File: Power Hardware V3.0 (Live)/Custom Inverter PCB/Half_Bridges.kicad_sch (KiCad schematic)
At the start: 27 parts, among them Q1 CSD19532Q5B, Q2 CSD19532Q5B, Q3 CSD19532Q5B, Q4 CSD19532Q5B, Q5 CSD19532Q5B, Q6 CSD19532Q5B

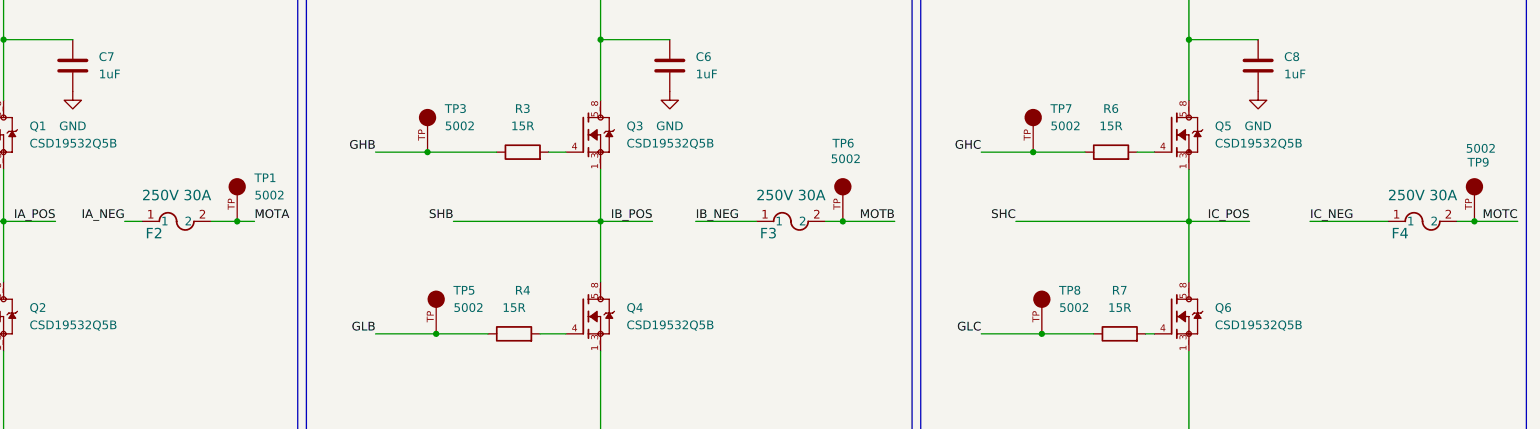
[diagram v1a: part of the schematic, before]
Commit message: PCB V3 changes
-HV outputs and inputs changed to screw terminals for lugs
- Fuses changes to 50A
- ADC pin for temp sense along with the temp sensing circuit
- Added more pins to motor encoder term for temp sense
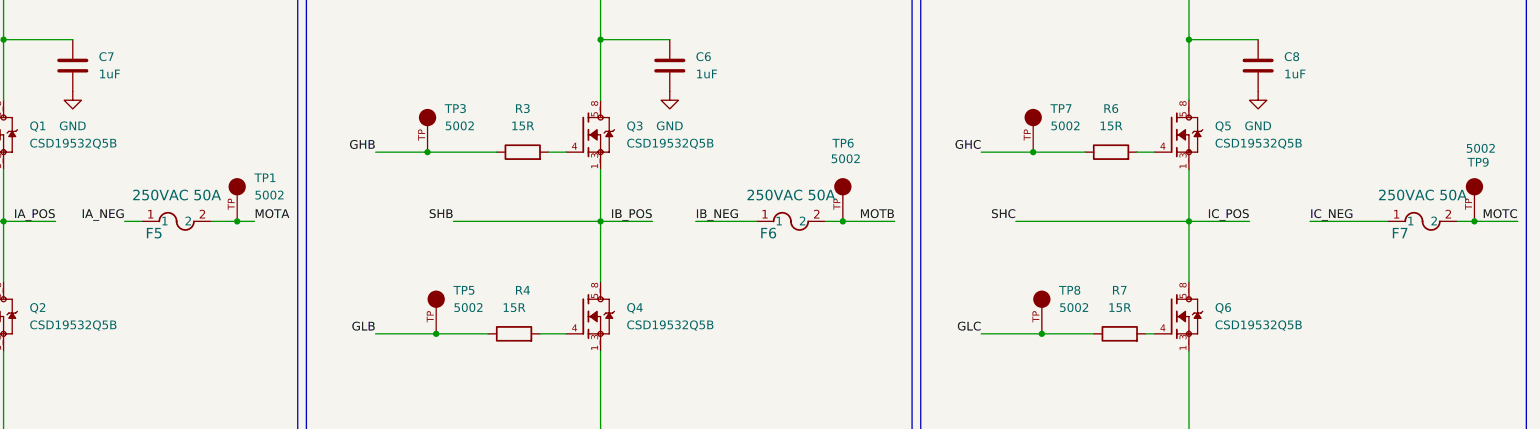
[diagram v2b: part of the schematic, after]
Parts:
- removed F2, F3, F4: 250V 30A, 0463030_ER:FUSE_0463_LTF-M, symbol 2025-02-24_21-09-15:0463030.ER
- added F5, F6, F7: 250VAC 50A, 0463030_ER:FUSE_0463_LTF-M, symbol 2025-02-24_21-09-15:0463030.ER
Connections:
- net IA_NEG: now also F5.1
- net IB_NEG: now also F6.1
- net IC_NEG: now also F7.1
- net MOTA: now also F5.2
- net MOTB: now also F6.2
- net MOTC: now also F7.2
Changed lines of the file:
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@@
-	)
-	(symbol
-		(lib_id "2025-02-24_21-09-15:0463030.ER")
-		(at 78.74 62.23 0)
-		(unit 1)
-		(exclude_from_sim no)
-		(in_bom yes)
-		(on_board yes)
-		(dnp no)
-		(property "Reference" "F2"
-			(at 80.518 64.008 0)
-			(effects
-				(font
-					(size 1.524 1.524)
-				)
-			)
-		)
-		(property "Value" "250V 30A"
-			(at 83.82 58.42 0)
-			(effects
-				(font
-					(size 1.524 1.524)
-				)
-			)
-		)
-		(property "Footprint" "0463030_ER:FUSE_0463_LTF-M"
-			(at 78.74 62.23 0)
-			(effects
-				(font
-					(size 1.27 1.27)
-					(italic yes)
-				)
-				(hide yes)
-			)
-		)
-		(property "Datasheet" "0463030.ER"
-			(at 78.74 62.23 0)
-			(effects
-				(font
-					(size 1.27 1.27)
-					(italic yes)
-				)
-				(hide yes)
-			)
-		)
-		(property "Description" "https://mm.digikey.com/Volume0/opasdata/d220001/medias/docus/1086/463_Series.pdf"
-			(at 78.74 62.23 0)
-			(effects
-				(font
-					(size 1.27 1.27)
-				)
-				(hide yes)
-			)
-		)
-		(property "Part Number" "0463030.ER"
-			(at 78.74 62.23 0)
-			(effects
-				(font
-					(size 1.27 1.27)
-				)
-				(hide yes)
-			)
-		)
-		(pin "2"
-		)
-		(pin "1"
-		)
-		(instances
-			(project "Custom Inverter PCB"
-				(path "/3e1046b6-e265-4cdd-8404-c358cfc105fe/dd00afae-8344-4250-8f9c-c68c6680e783"
-					(reference "F2")
-					(unit 1)
-				)
-			)
-		)
 	)
 	(symbol
@@
 	(symbol
 		(lib_id "2025-02-24_21-09-15:0463030.ER")
-		(at 168.91 62.23 0)
-		(unit 1)
-		(exclude_from_sim no)
-		(in_bom yes)
-		(on_board yes)
-		(dnp no)
-		(property "Reference" "F3"
-			(at 170.688 64.008 0)
+		(at 78.74 62.23 0)
+		(unit 1)
+		(exclude_from_sim no)
+		(in_bom yes)
+		(on_board yes)
+		(dnp no)
+		(property "Reference" "F5"
+			(at 80.518 64.008 0)
 			(effects
 				(font
@@
 			)
 		)
-		(property "Value" "250V 30A"
-			(at 173.99 58.42 0)
+		(property "Value" "250VAC 50A"
+			(at 83.82 58.42 0)
 			(effects
 				(font
@@
 		)
 		(property "Footprint" "0463030_ER:FUSE_0463_LTF-M"
-			(at 168.91 62.23 0)
+			(at 78.74 62.23 0)
 			(effects
 				(font
@@
 			)
 		)
-		(property "Datasheet" "0463030.ER"
-			(at 168.91 62.23 0)
+		(property "Datasheet" "https://www.bourns.com/docs/Product-Datasheets/SF-3812F-T.pdf"
+			(at 78.74 62.23 0)
 			(effects
 				(font
@@
 			)
 		)
-		(property "Description" "https://mm.digikey.com/Volume0/opasdata/d220001/medias/docus/1086/463_Series.pdf"
-			(at 168.91 62.23 0)
-			(effects
-				(font
-					(size 1.27 1.27)
-				)
-				(hide yes)
-			)
-		)
-		(property "Part Number" "0463030.ER"
-			(at 168.91 62.23 0)
+		(property "Description" "50A 250VAC, 100VDC"
+			(at 78.74 62.23 0)
+			(effects
+				(font
+					(size 1.27 1.27)
+				)
+				(hide yes)
+			)
+		)
+		(property "Part Number" "SF-3812F5000T-2"
+			(at 78.74 62.23 0)
 			(effects
 				(font
@@
 			(project "Custom Inverter PCB"
 				(path "/3e1046b6-e265-4cdd-8404-c358cfc105fe/dd00afae-8344-4250-8f9c-c68c6680e783"
-					(reference "F3")
+					(reference "F5")
 					(unit 1)
 				)
@@
 	)
 	(symbol
+		(lib_id "2025-02-24_21-09-15:0463030.ER")
+		(at 168.91 62.23 0)
+		(unit 1)
+		(exclude_from_sim no)
+		(in_bom yes)
+		(on_board yes)
+		(dnp no)
+		(property "Reference" "F6"
+			(at 170.688 64.008 0)
+			(effects
+				(font
+					(size 1.524 1.524)
+				)
+			)
+		)
+		(property "Value" "250VAC 50A"
+			(at 173.99 58.42 0)
+			(effects
+				(font
+					(size 1.524 1.524)
+				)
+			)
+		)
+		(property "Footprint" "0463030_ER:FUSE_0463_LTF-M"
+			(at 168.91 62.23 0)
+			(effects
+				(font
+					(size 1.27 1.27)
+					(italic yes)
+				)
+				(hide yes)
+			)
+		)
+		(property "Datasheet" "https://www.bourns.com/docs/Product-Datasheets/SF-3812F-T.pdf"
+			(at 168.91 62.23 0)
+			(effects
+				(font
+					(size 1.27 1.27)
+					(italic yes)
+				)
+				(hide yes)
+			)
+		)
+		(property "Description" "50A 250VAC, 100VDC"
+			(at 168.91 62.23 0)
+			(effects
+				(font
+					(size 1.27 1.27)
+				)
+				(hide yes)
+			)
+		)
+		(property "Part Number" "SF-3812F5000T-2"
+			(at 168.91 62.23 0)
+			(effects
+				(font
+					(size 1.27 1.27)
+				)
+				(hide yes)
+			)
+		)
+		(pin "2"
+		)
+		(pin "1"
+		)
+		(instances
+			(project "Custom Inverter PCB"
+				(path "/3e1046b6-e265-4cdd-8404-c358cfc105fe/dd00afae-8344-4250-8f9c-c68c6680e783"
+					(reference "F6")
+					(unit 1)
+				)
+			)
+		)
+	)
+	(symbol
 		(lib_id "5002:5002")
 		(at 121.92 73.66 90)
@@
 	)
 	(symbol
+		(lib_id "2025-02-24_21-09-15:0463030.ER")
+		(at 261.62 62.23 0)
+		(unit 1)
+		(exclude_from_sim no)
+		(in_bom yes)
+		(on_board yes)
+		(dnp no)
+		(property "Reference" "F7"
+			(at 263.398 64.008 0)
+			(effects
+				(font
+					(size 1.524 1.524)
+				)
+			)
+		)
+		(property "Value" "250VAC 50A"
+			(at 266.7 58.42 0)
+			(effects
+				(font
+					(size 1.524 1.524)
+				)
+			)
+		)
+		(property "Footprint" "0463030_ER:FUSE_0463_LTF-M"
+			(at 261.62 62.23 0)
+			(effects
+				(font
+					(size 1.27 1.27)
+					(italic yes)
+				)
+				(hide yes)
+			)
+		)
+		(property "Datasheet" "https://www.bourns.com/docs/Product-Datasheets/SF-3812F-T.pdf"
+			(at 261.62 62.23 0)
+			(effects
+				(font
+					(size 1.27 1.27)
+					(italic yes)
+				)
+				(hide yes)
+			)
+		)
+		(property "Description" "50A 250VAC, 100VDC"
+			(at 261.62 62.23 0)
+			(effects
+				(font
+					(size 1.27 1.27)
+				)
+				(hide yes)
+			)
+		)
+		(property "Part Number" "SF-3812F5000T-2"
+			(at 261.62 62.23 0)
+			(effects
+				(font
+					(size 1.27 1.27)
+				)
+				(hide yes)
+			)
+		)
+		(pin "2"
+		)
+		(pin "1"
+		)
+		(instances
+			(project "Custom Inverter PCB"
+				(path "/3e1046b6-e265-4cdd-8404-c358cfc105fe/dd00afae-8344-4250-8f9c-c68c6680e783"
+					(reference "F7")
+					(unit 1)
+				)
+			)
+		)
+	)
+	(symbol
 		(lib_id "5002:5002")
 		(at 120.65 46.99 90)
@@
 					(unit 1)
 				)
-			)
-		)
-	)
-	(symbol
-		(lib_id "2025-02-24_21-09-15:0463030.ER")
-		(at 261.62 62.23 0)
-		(unit 1)
-		(exclude_from_sim no)
-		(in_bom yes)
-		(on_board yes)
-		(dnp no)
-		(property "Reference" "F4"
-			(at 263.398 64.008 0)
-			(effects
-				(font
-					(size 1.524 1.524)
-				)
-			)
-		)
-		(property "Value" "250V 30A"
-			(at 266.7 58.42 0)
-			(effects
-				(font
-					(size 1.524 1.524)
-				)
-			)
-		)
-		(property "Footprint" "0463030_ER:FUSE_0463_LTF-M"
-			(at 261.62 62.23 0)
-			(effects
-				(font
-					(size 1.27 1.27)
-					(italic yes)
-				)
-				(hide yes)
-			)
-		)
-		(property "Datasheet" "https://mm.digikey.com/Volume0/opasdata/d220001/medias/docus/1086/463_Series.pdf"
-			(at 261.62 62.23 0)
-			(effects
-				(font
-					(size 1.27 1.27)
-					(italic yes)
-				)
-				(hide yes)
-			)
-		)
-		(property "Description" ""
-			(at 261.62 62.23 0)
-			(effects
-				(font
-					(size 1.27 1.27)
-				)
-				(hide yes)
-			)
-		)
-		(property "Part Number" "0463030.ER"
-			(at 261.62 62.23 0)
-			(effects
-				(font
-					(size 1.27 1.27)
-				)
-				(hide yes)
-			)
-		)
-		(pin "2"
-		)
-		(pin "1"
-		)
-		(instances
-			(project "Custom Inverter PCB"
-				(path "/3e1046b6-e265-4cdd-8404-c358cfc105fe/dd00afae-8344-4250-8f9c-c68c6680e783"
-					(reference "F4")
-					(unit 1)
-				)

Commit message: PCB layout
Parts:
- removed Q1, Q2, Q3, Q4, Q5, Q6: CSD19532Q5B, CSD19532Q5B:TRANS_CSD19532Q5B, symbol CSD19532Q5B:CSD19532Q5B
- added Q1, Q2, Q3, Q4, Q5, Q6: IRFB4115PBF, Package_TO_SOT_THT:TO-220-3_Vertical, symbol Device:Q_NMOS
- renumbered C6 to C8, C8 to C9, F5 to F2, F6 to F3, F7 to F4, R1 to R3, R2 to R4, R4 to R5, R3 to R6, R6 to R7, R7 to R8, TP2 to TP1, TP4 to TP2, TP1 to TP3, TP3 to TP4
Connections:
- net +100VDC: now also Q1.2 (D), Q3.2 (D), Q5.2 (D)
- net GND: now also Q2.3 (S), Q4.3 (S), Q6.3 (S)
- net IA_POS: now also Q1.3 (S), Q2.2 (D)
- net IB_POS: now also Q3.3 (S), Q4.2 (D)
- net IC_POS: now also Q5.3 (S), Q6.2 (D)
- net at R3.2: now also Q1.1 (G)
- net at R4.2: now also Q2.1 (G)
- net at R7.2: now also Q5.1 (G)
- net at R8.2: now also Q6.1 (G)
- net at R6.2: now also Q3.1 (G)
- net at R5.2: now also Q4.1 (G)
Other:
- moved on the sheet: R3, R4, R5, R6, R7, R8, TP1, TP2, TP4, TP5, TP7, TP8

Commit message: changes
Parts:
- TP1, TP2, TP3, TP4, TP5, TP6, TP7, TP8, TP9: Part Number (none) -> 5002
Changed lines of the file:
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@@
 			)
 		)
-		(property "Part Number" ""
+		(property "Part Number" "5002"
 			(at 274.32 57.15 0)
 			(effects
@@
 			)
 		)
-		(property "Part Number" ""
+		(property "Part Number" "5002"
 			(at 92.71 57.15 0)
 			(effects
@@
 			)
 		)
-		(property "Part Number" ""
+		(property "Part Number" "5002"
 			(at 30.48 69.85 0)
 			(effects
@@
 			)
 		)
-		(property "Part Number" ""
+		(property "Part Number" "5002"
 			(at 208.28 44.45 0)
 			(effects
@@
 			)
 		)
-		(property "Part Number" ""
+		(property "Part Number" "5002"
 			(at 30.48 44.45 0)
 			(effects
@@
 			)
 		)
-		(property "Part Number" ""
+		(property "Part Number" "5002"
 			(at 119.38 71.12 0)
 			(effects
@@
 			)
 		)
-		(property "Part Number" ""
+		(property "Part Number" "5002"
 			(at 181.61 57.15 0)
 			(effects
@@
 			)
 		)
-		(property "Part Number" ""
+		(property "Part Number" "5002"
 			(at 208.28 71.12 0)
 			(effects
@@
 			)
 		)
-		(property "Part Number" ""
+		(property "Part Number" "5002"
 			(at 119.38 43.18 0)
 			(effects
